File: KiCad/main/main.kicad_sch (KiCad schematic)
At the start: 39 parts, among them J1 Hexpansion-Connector, J2 Conn_01x04_Socket, U1 TCA8418, U2 AP3032AKTR, U4 ZD24C64A-XGMT

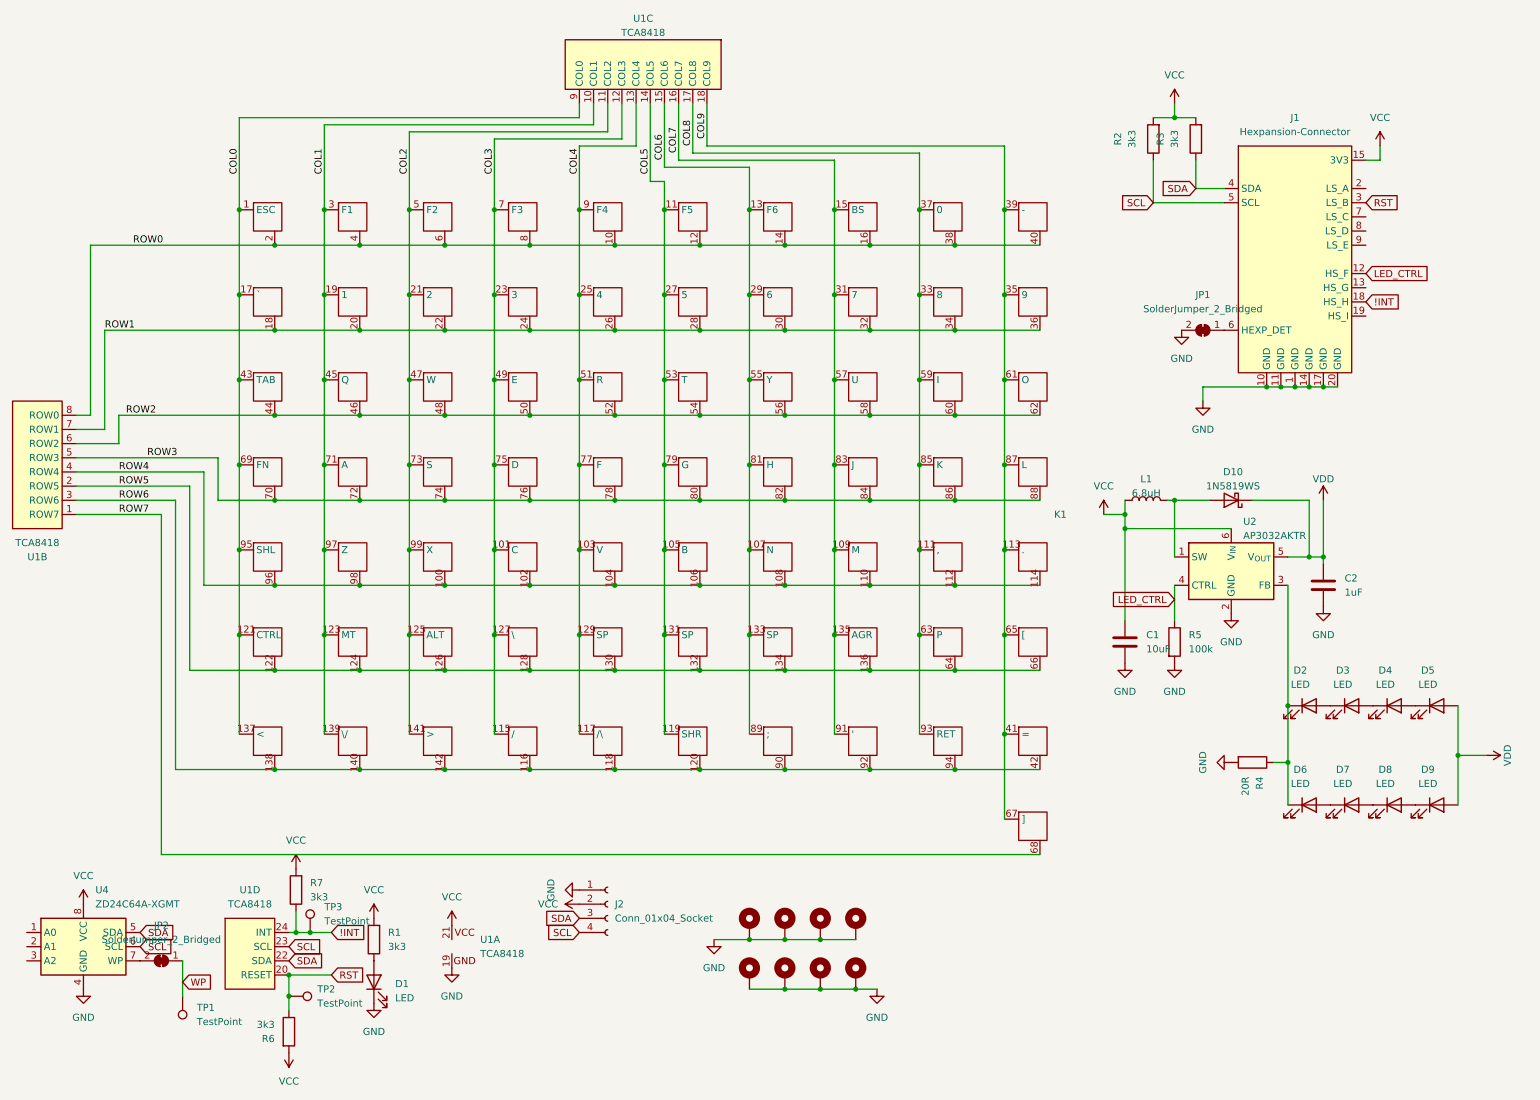
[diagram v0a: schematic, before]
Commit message: Modify for EMF camp - Change shape - Move standoffs to bottom PCB - Add RGB LEDs and power conversion for them - Add art - Generate and add 3D models
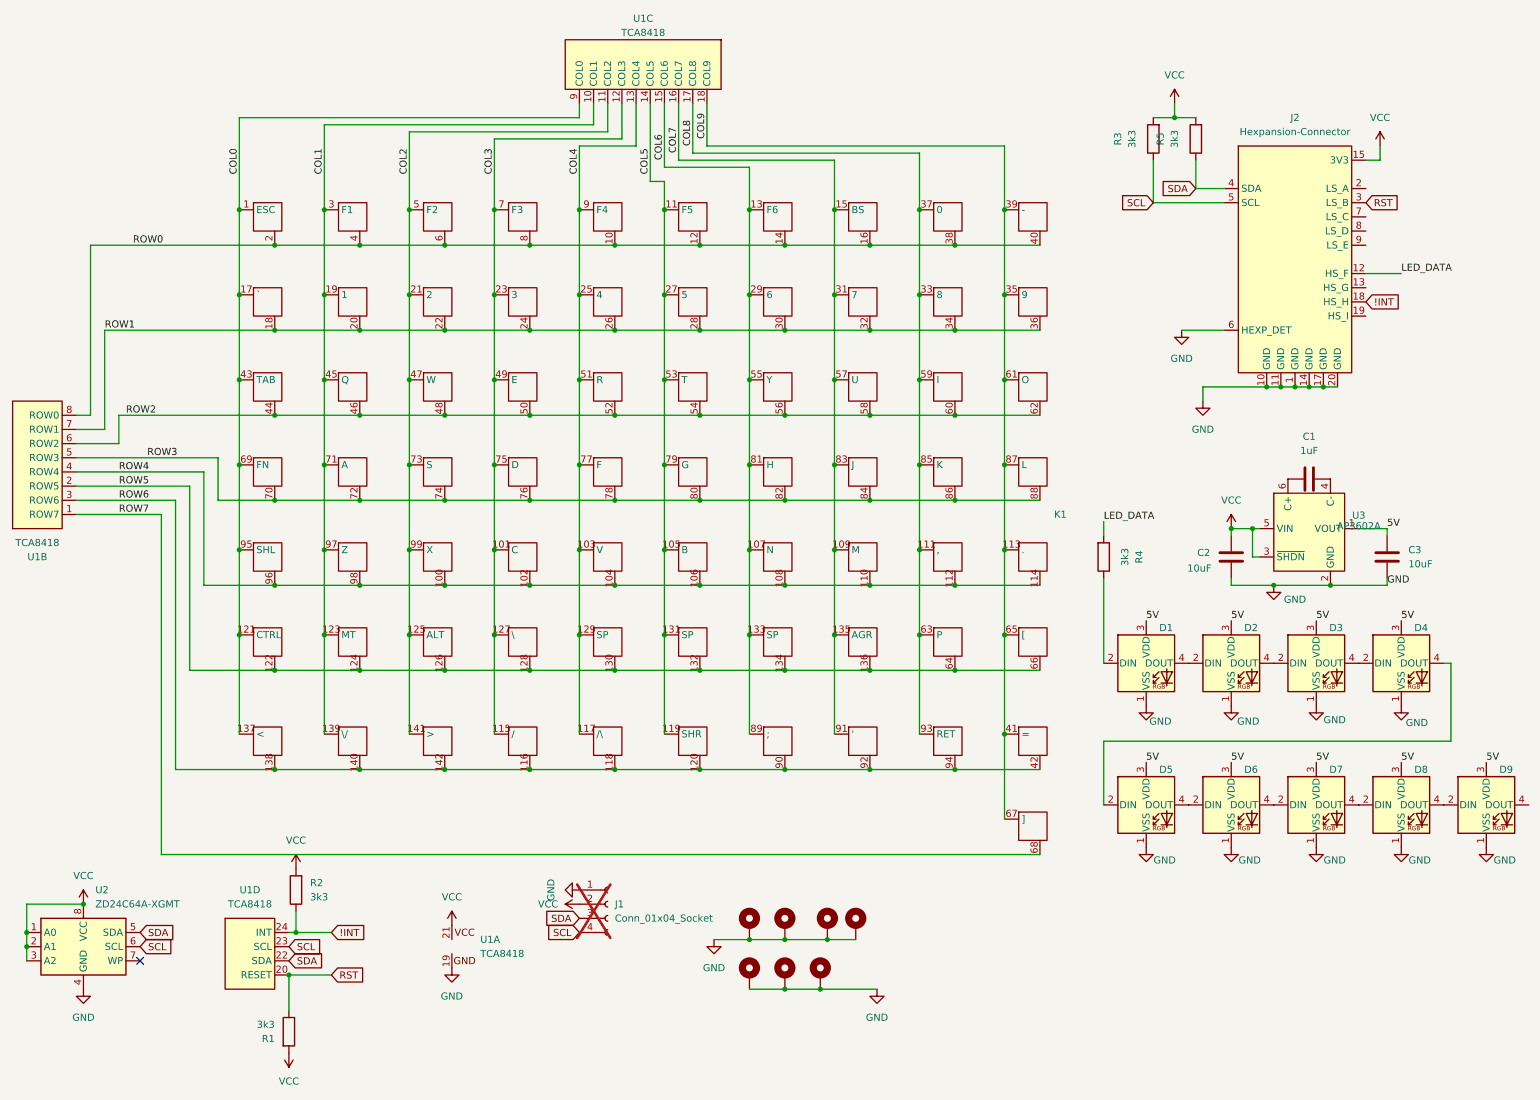
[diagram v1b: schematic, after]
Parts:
- removed D1: LED, LED_SMD:LED_0603_1608Metric_Pad1.05x0.95mm_HandSolder, symbol Device:LED
- removed D10: 1N5819WS, Diode_SMD:D_SOD-323, symbol Diode:1N5819WS
- removed D2, D3, D4, D5, D6, D7, D8, D9: LED, keyboard_leds:LTW-010DCG, symbol Device:LED
- removed H3, H4: MountingHole_Pad, MountingHole:MountingHole_2.2mm_M2_Pad_Via, symbol Mechanical:MountingHole_Pad
- removed JP1, JP2: SolderJumper_2_Bridged, Jumper:SolderJumper-2_P1.3mm_Bridged_RoundedPad1.0x1.5mm, symbol Jumper:SolderJumper_2_Bridged
- removed L1: 6.8uH, Inductor_SMD:L_0603_1608Metric_Pad1.05x0.95mm_HandSolder, symbol Device:L
- removed R1: 3k3, Resistor_SMD:R_0603_1608Metric_Pad0.98x0.95mm_HandSolder, symbol Device:R
- removed R5: 100k, Resistor_SMD:R_0603_1608Metric_Pad0.98x0.95mm_HandSolder, symbol Device:R
- removed TP1, TP2, TP3: TestPoint, TestPoint:TestPoint_Pad_D1.5mm, symbol Connector:TestPoint
- removed U2: AP3032AKTR, Package_TO_SOT_SMD:SOT-23-6, symbol Driver_LED:AP3019AKTR
- added C3: 10uF, Capacitor_SMD:C_0603_1608Metric, symbol Device:C
- added D1, D2, D3, D4, D5, D6, D7, D8, D9: XL-3210RGBC-WS2812B, tildagon:XL-3210RGBC-2812B, symbol tildagon:SK6805SIDE-S
- added H7: SMTSO2020CTJ, frontplate:SMTSO2020CTJ, symbol Mechanical:MountingHole_Pad
- added U3: AP3602A, Package_TO_SOT_SMD:TSOT-23-6_HandSoldering, symbol AP3602:AP3602A
- C1: value 10uF -> 1uF; footprint Capacitor_SMD:C_0603_1608Metric_Pad1.08x0.95mm_HandSolder -> Capacitor_SMD:C_0402_1005Metric; MPN (none) -> C2887021
- C2: value 1uF -> 10uF; footprint Capacitor_SMD:C_0603_1608Metric_Pad1.08x0.95mm_HandSolder -> Capacitor_SMD:C_0603_1608Metric; MPN (none) -> C3015157
- H2: renamed from H5; value MountingHole_Pad -> SMTSO2020CTJ; footprint MountingHole:MountingHole_2.2mm_M2_Pad_Via -> frontplate:SMTSO2020CTJ
- H4: renamed from H6; value MountingHole_Pad -> SMTSO2020CTJ; footprint MountingHole:MountingHole_2.2mm_M2_Pad_Via -> frontplate:SMTSO2020CTJ
- H5: renamed from H7; value MountingHole_Pad -> SMTSO2020CTJ; footprint MountingHole:MountingHole_2.2mm_M2_Pad_Via -> frontplate:SMTSO2020CTJ
- H6: renamed from H8; value MountingHole_Pad -> SMTSO2020CTJ; footprint MountingHole:MountingHole_2.2mm_M2_Pad_Via -> frontplate:SMTSO2020CTJ
- J1: renamed from J2; now not fitted
- R4: value 20R -> 3k3
- U1: footprint TCA8418RTWR:QFN50P400X400X80-25N -> Package_DFN_QFN:WQFN-24-1EP_4x4mm_P0.5mm_EP2.45x2.45mm
- renumbered H2 to H3, J1 to J2, R6 to R1, R7 to R2, R2 to R3, R3 to R5, U4 to U2
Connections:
- net VDD is gone; now on net GND: C2.1
- net GND: now also J2.6 (HEXP_DET), C3.1, D1.1 (VSS), D2.1 (VSS), D3.1 (VSS), D4.1 (VSS), D5.1 (VSS), D6.1 (VSS), D7.1 (VSS), D8.1 (VSS), D9.1 (VSS), H7.1, U3.2 (GND); no longer C1.2, C2.2, R4.2
- net VCC: now also C2.2, U2.1 (A0), U2.2 (A1), U2.3 (A2), U3.3 (~{SHDN}), U3.5 (VIN); no longer C1.1
- net at R4.1: now also D1.2 (DIN)
- net LED_CTRL renamed LED_DATA
- net LED_DATA: now also R4.2
- new net: C1.2, U3.4 (C-)
- new net: C1.1, U3.6 (C+)
- new net: D3.4 (DOUT), D4.2 (DIN)
- new net: D4.4 (DOUT), D5.2 (DIN)
- new net: D6.4 (DOUT), D7.2 (DIN)
- new net: D7.4 (DOUT), D8.2 (DIN)
- new net: D8.4 (DOUT), D9.2 (DIN)
- new net: D5.4 (DOUT), D6.2 (DIN)
- new net: D1.4 (DOUT), D2.2 (DIN)
- new net: D2.4 (DOUT), D3.2 (DIN)
- new net 5V: C3.2, D1.3 (VDD), D2.3 (VDD), D3.3 (VDD), D4.3 (VDD), D5.3 (VDD), D6.3 (VDD), D7.3 (VDD), D8.3 (VDD), D9.3 (VDD), U3.1 (VOUT)
- no-connect marks 0 -> 1
